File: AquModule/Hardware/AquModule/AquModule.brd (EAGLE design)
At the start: 100 x 80 mm, 22 parts

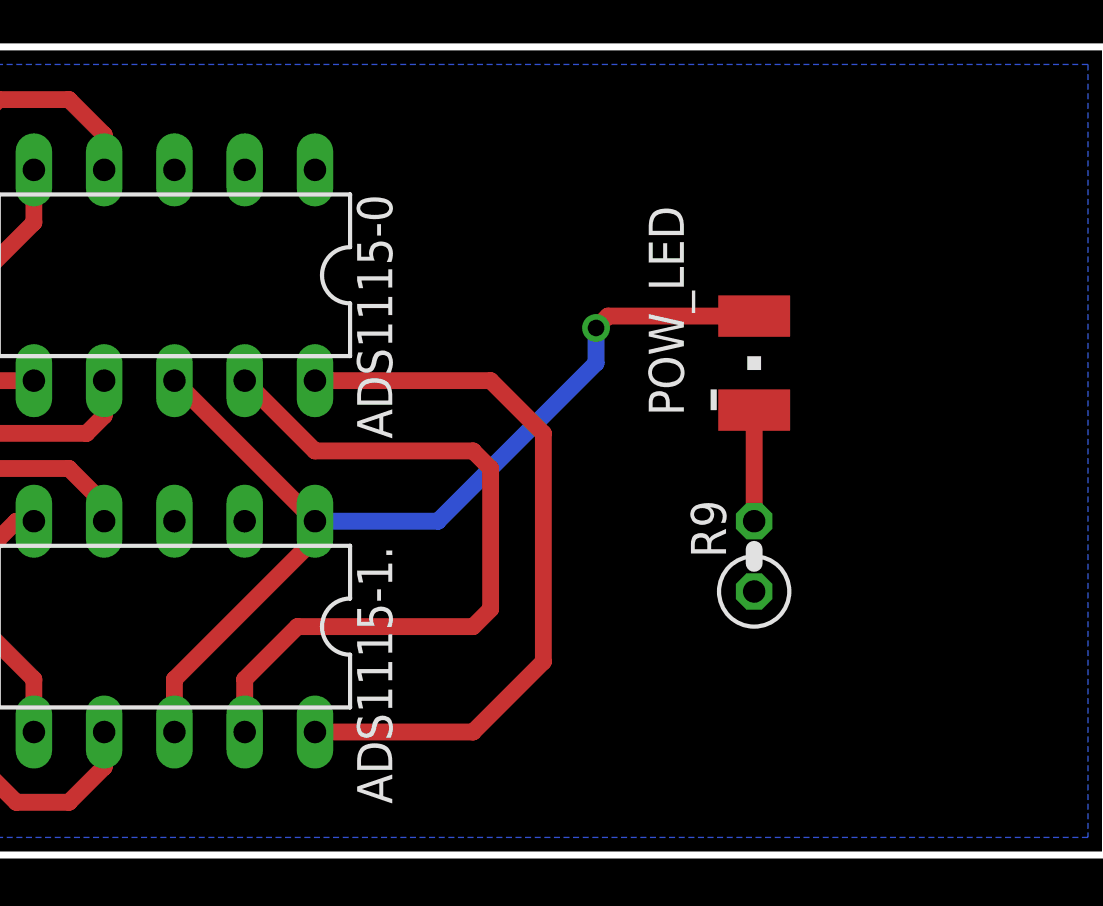
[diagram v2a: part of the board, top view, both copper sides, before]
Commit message: PCB ADD0 and ADD1 ready
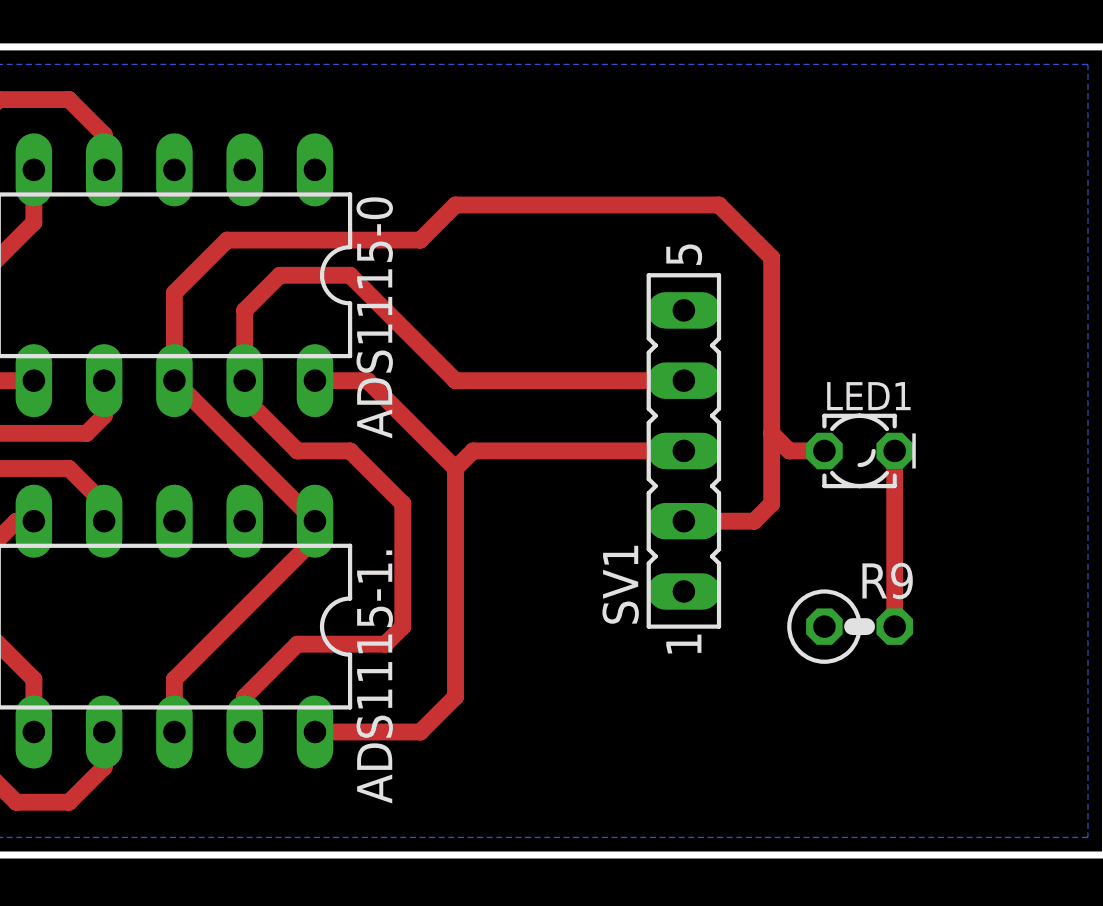
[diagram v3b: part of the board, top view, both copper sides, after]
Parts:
- removed POW_LED: LS_T679-D2E2-1, led:PLCC2
- added LED1: (no value), eagle-ltspice:LED_LD260
- added SV1: (no value), con-lsta:FE05-1
- moved R9 4.58 mm to (82.5, 38.7), turned to 0 degrees
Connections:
- net GND: now also SV1.5
- net N$17: now also LED1.K; no longer POW_LED.C
- net SCL: now also SV1.3
- net SDA: now also SV1.4
- net VCC: now also LED1.A, SV1.2; no longer POW_LED.A
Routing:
- net VCC: track 36.6 -> 58.3 mm, vias 1 -> 0
- net SDA: track 27.1 -> 40.9 mm
- net N$17: track 4.02 -> 6.35 mm
- net SCL: track 26.6 -> 28.8 mm
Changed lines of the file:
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@@
 <layer number="97" name="Info" color="7" fill="1" visible="no" active="no"/>
 <layer number="98" name="Guide" color="6" fill="1" visible="no" active="no"/>
+<layer number="99" name="SpiceOrder" color="5" fill="1" visible="no" active="no"/>
 </layers>
 <board>
@@
 <element name="C7" library="rcl" package="C1005" value="100nF" x="37.465" y="51.435" rot="MR180"/>
 <element name="C8" library="rcl" package="C1005" value="100nF" x="37.465" y="53.975" rot="MR180"/>
-<element name="POW_LED" library="led" package="PLCC2" value="LS_T679-D2E2-1" x="78.74" y="48.26">
-<attribute name="COLOR" value="super-red" x="78.74" y="48.26" size="1.778" layer="27" display="off"/>
+<element name="R9" library="resistor" package="0207/2V" value="?" x="82.55" y="38.735"/>
+<element name="SV1" library="con-lsta" package="FE05-1" value="" x="76.2" y="45.085" rot="R90">
+<attribute name="OC_NEWARK" value="unknown" x="76.2" y="45.085" size="1.778" layer="27" rot="R90" display="off"/>
+<attribute name="MPN" value="" x="76.2" y="45.085" size="1.778" layer="27" rot="R90" display="off"/>
+<attribute name="MF" value="" x="76.2" y="45.085" size="1.778" layer="27" rot="R90" display="off"/>
+<attribute name="OC_FARNELL" value="unknown" x="76.2" y="45.085" size="1.778" layer="27" rot="R90" display="off"/>
 </element>
-<element name="R9" library="resistor" package="0207/2V" value="?" x="78.74" y="41.275" rot="R90"/>
+<element name="LED1" library="eagle-ltspice" package="LED_LD260" value="" x="82.55" y="45.085">
+<attribute name="SPICEMODEL" value="NONE" x="82.55" y="45.085" size="1.778" layer="27" display="off"/>
+<attribute name="SPICETYPE" value="diode" x="82.55" y="45.085" size="1.778" layer="27" display="off"/>
+<attribute name="SPICEPREFIX" value="D" x="82.55" y="45.085" size="1.778" layer="27" display="off"/>
+</element>
 </elements>
 <signals>
@@
 </polygon>
 <contactref element="R9" pad="1"/>
+<contactref element="SV1" pad="5"/>
 </signal>
 <signal name="VCC">
@@
 <wire x1="62.865" y1="41.91" x2="57.785" y2="36.83" width="0.6096" layer="1"/>
 <wire x1="57.785" y1="36.83" x2="57.785" y2="34.925" width="0.6096" layer="1"/>
-<contactref element="POW_LED" pad="A"/>
-<wire x1="78.74" y1="49.96" x2="73.455" y2="49.96" width="0.6096" layer="1"/>
-<wire x1="73.455" y1="49.96" x2="73.025" y2="49.53" width="0.6096" layer="1"/>
-<via x="73.025" y="49.53" extent="1-16" drill="0.6" shape="square"/>
-<wire x1="73.025" y1="49.53" x2="73.025" y2="48.26" width="0.6096" layer="16"/>
-<wire x1="73.025" y1="48.26" x2="67.31" y2="42.545" width="0.6096" layer="16"/>
-<wire x1="67.31" y1="42.545" x2="62.865" y2="42.545" width="0.6096" layer="16"/>
+<contactref element="SV1" pad="2"/>
+<wire x1="76.2" y1="42.545" x2="78.74" y2="42.545" width="0.6096" layer="1"/>
+<wire x1="78.74" y1="42.545" x2="79.375" y2="43.18" width="0.6096" layer="1"/>
+<wire x1="79.375" y1="43.18" x2="79.375" y2="45.72" width="0.6096" layer="1"/>
+<wire x1="79.375" y1="45.72" x2="79.375" y2="52.07" width="0.6096" layer="1"/>
+<wire x1="79.375" y1="52.07" x2="77.47" y2="53.975" width="0.6096" layer="1"/>
+<wire x1="77.47" y1="53.975" x2="67.945" y2="53.975" width="0.6096" layer="1"/>
+<wire x1="67.945" y1="53.975" x2="66.675" y2="52.705" width="0.6096" layer="1"/>
+<wire x1="66.675" y1="52.705" x2="59.69" y2="52.705" width="0.6096" layer="1"/>
+<wire x1="59.69" y1="52.705" x2="57.785" y2="50.8" width="0.6096" layer="1"/>
+<wire x1="57.785" y1="50.8" x2="57.785" y2="47.625" width="0.6096" layer="1"/>
+<contactref element="LED1" pad="A"/>
+<wire x1="81.28" y1="45.085" x2="80.01" y2="45.085" width="0.6096" layer="1"/>
+<wire x1="80.01" y1="45.085" x2="79.375" y2="45.72" width="0.6096" layer="1"/>
 </signal>
 <signal name="SCL">
 <contactref element="ADS1115-0" pad="10"/>
 <contactref element="ADS1115-1." pad="10"/>
-<wire x1="62.865" y1="47.625" x2="69.215" y2="47.625" width="0.6096" layer="1"/>
-<wire x1="69.215" y1="47.625" x2="71.12" y2="45.72" width="0.6096" layer="1"/>
-<wire x1="71.12" y1="45.72" x2="71.12" y2="37.465" width="0.6096" layer="1"/>
-<wire x1="71.12" y1="37.465" x2="68.58" y2="34.925" width="0.6096" layer="1"/>
-<wire x1="68.58" y1="34.925" x2="62.865" y2="34.925" width="0.6096" layer="1"/>
+<contactref element="SV1" pad="3"/>
+<wire x1="62.865" y1="47.625" x2="64.77" y2="47.625" width="0.6096" layer="1"/>
+<wire x1="64.77" y1="47.625" x2="67.945" y2="44.45" width="0.6096" layer="1"/>
+<wire x1="67.945" y1="44.45" x2="67.945" y2="36.195" width="0.6096" layer="1"/>
+<wire x1="67.945" y1="36.195" x2="66.675" y2="34.925" width="0.6096" layer="1"/>
+<wire x1="66.675" y1="34.925" x2="62.865" y2="34.925" width="0.6096" layer="1"/>
+<wire x1="76.2" y1="45.085" x2="68.58" y2="45.085" width="0.6096" layer="1"/>
+<wire x1="68.58" y1="45.085" x2="67.945" y2="44.45" width="0.6096" layer="1"/>
 </signal>
 <signal name="SDA">
 <contactref element="ADS1115-0" pad="9"/>
 <contactref element="ADS1115-1." pad="9"/>
-<wire x1="60.325" y1="47.625" x2="62.865" y2="45.085" width="0.6096" layer="1"/>
-<wire x1="62.865" y1="45.085" x2="68.58" y2="45.085" width="0.6096" layer="1"/>
-<wire x1="68.58" y1="45.085" x2="69.215" y2="44.45" width="0.6096" layer="1"/>
-<wire x1="69.215" y1="44.45" x2="69.215" y2="39.37" width="0.6096" layer="1"/>
-<wire x1="69.215" y1="39.37" x2="68.58" y2="38.735" width="0.6096" layer="1"/>
-<wire x1="68.58" y1="38.735" x2="62.23" y2="38.735" width="0.6096" layer="1"/>
-<wire x1="62.23" y1="38.735" x2="60.325" y2="36.83" width="0.6096" layer="1"/>
-<wire x1="60.325" y1="36.83" x2="60.325" y2="34.925" width="0.6096" layer="1"/>
+<contactref element="SV1" pad="4"/>
+<wire x1="60.325" y1="47.625" x2="60.325" y2="46.99" width="0.6096" layer="1"/>
+<wire x1="60.325" y1="46.99" x2="62.23" y2="45.085" width="0.6096" layer="1"/>
+<wire x1="62.23" y1="45.085" x2="64.135" y2="45.085" width="0.6096" layer="1"/>
+<wire x1="64.135" y1="45.085" x2="66.04" y2="43.18" width="0.6096" layer="1"/>
+<wire x1="66.04" y1="43.18" x2="66.04" y2="38.735" width="0.6096" layer="1"/>
+<wire x1="66.04" y1="38.735" x2="65.405" y2="38.1" width="0.6096" layer="1"/>
+<wire x1="65.405" y1="38.1" x2="62.23" y2="38.1" width="0.6096" layer="1"/>
+<wire x1="62.23" y1="38.1" x2="60.325" y2="36.195" width="0.6096" layer="1"/>
+<wire x1="60.325" y1="36.195" x2="60.325" y2="34.925" width="0.6096" layer="1"/>
+<wire x1="76.2" y1="47.625" x2="67.945" y2="47.625" width="0.6096" layer="1"/>
+<wire x1="67.945" y1="47.625" x2="64.135" y2="51.435" width="0.6096" layer="1"/>
+<wire x1="64.135" y1="51.435" x2="61.595" y2="51.435" width="0.6096" layer="1"/>
+<wire x1="61.595" y1="51.435" x2="60.325" y2="50.165" width="0.6096" layer="1"/>
+<wire x1="60.325" y1="50.165" x2="60.325" y2="47.625" width="0.6096" layer="1"/>
 </signal>
 <signal name="N$9">
@@
 </signal>
 <signal name="N$17">
-<contactref element="POW_LED" pad="C"/>
 <contactref element="R9" pad="2"/>
-<wire x1="78.74" y1="46.56" x2="78.74" y2="42.545" width="0.6096" layer="1"/>
+<contactref element="LED1" pad="K"/>
+<wire x1="83.82" y1="45.085" x2="83.82" y2="38.735" width="0.6096" layer="1"/>
 </signal>
 </signals>

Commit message: Aqu Module 2 PCB - Ready
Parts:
- LED1: value (none) -> GREEN
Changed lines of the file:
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@@
 <layer number="43" name="vRestrict" color="2" fill="10" visible="yes" active="yes"/>
 <layer number="44" name="Drills" color="7" fill="1" visible="no" active="yes"/>
-<layer number="45" name="Holes" color="7" fill="1" visible="no" active="yes"/>
+<layer number="45" name="Holes" color="7" fill="1" visible="yes" active="yes"/>
 <layer number="46" name="Milling" color="3" fill="1" visible="yes" active="yes"/>
 <layer number="47" name="Measures" color="7" fill="1" visible="no" active="yes"/>
@@
 <wire x1="13.97" y1="30.48" x2="13.97" y2="59.69" width="0.254" layer="46"/>
 <wire x1="21.59" y1="59.69" x2="21.59" y2="30.48" width="0.254" layer="46"/>
+<hole x="27.94" y="55.245" drill="0.6"/>
 </plain>
 <attributes>
@@
 <attribute name="OC_FARNELL" value="unknown" x="76.2" y="45.085" size="1.778" layer="27" rot="R90" display="off"/>
 </element>
-<element name="LED1" library="eagle-ltspice" package="LED_LD260" value="" x="82.55" y="45.085">
+<element name="LED1" library="eagle-ltspice" package="LED_LD260" value="GREEN" x="82.55" y="45.085">
 <attribute name="SPICEMODEL" value="NONE" x="82.55" y="45.085" size="1.778" layer="27" display="off"/>
 <attribute name="SPICETYPE" value="diode" x="82.55" y="45.085" size="1.778" layer="27" display="off"/>
